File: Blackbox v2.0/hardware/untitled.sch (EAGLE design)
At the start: 40 parts, among them IC1 MEGA8-AI, IC2 7805DT, Q1 CSM-7X-DU

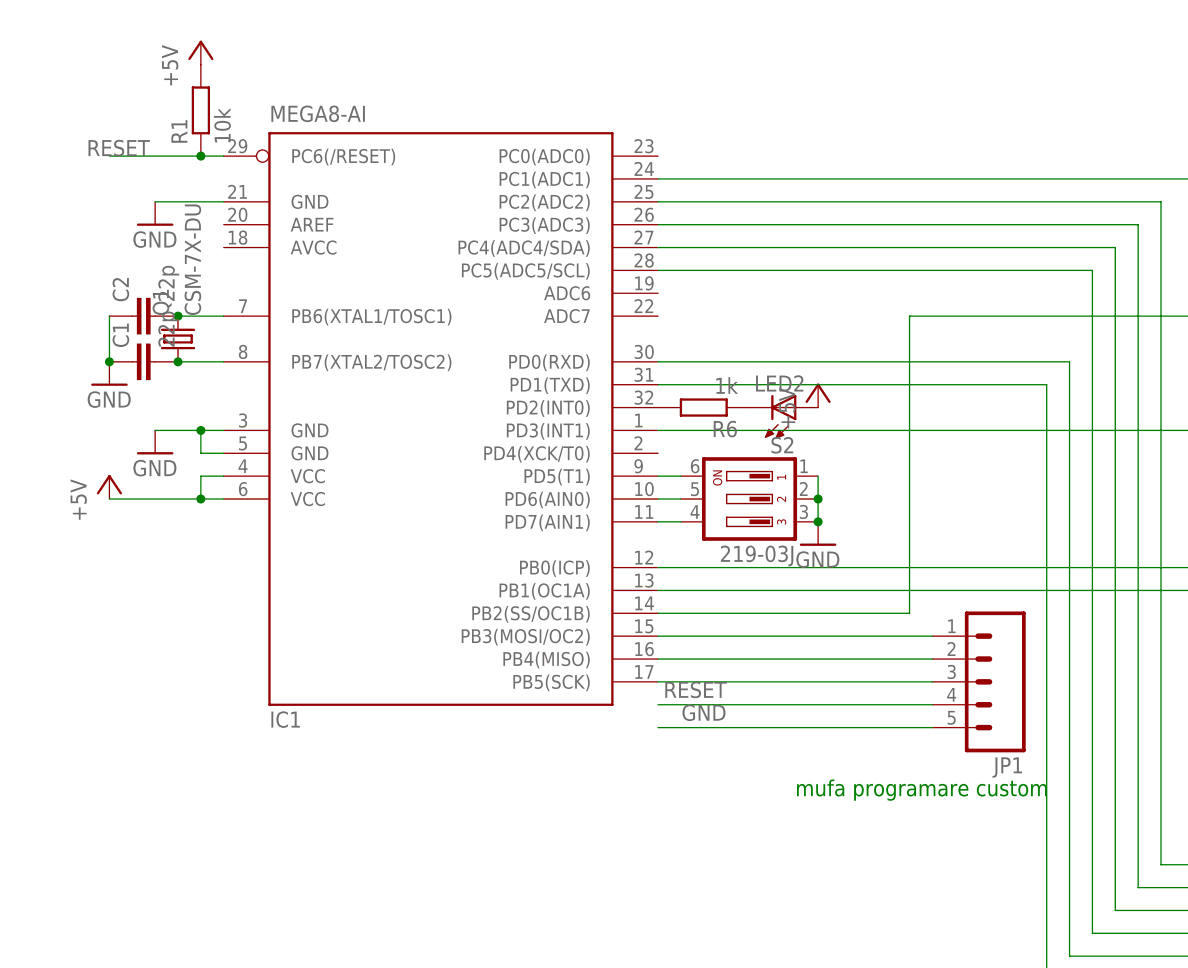
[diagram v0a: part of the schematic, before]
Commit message: Adaug placa in versiunea noua
(mufa de programare cu 6 pini si condensator pt ADC)
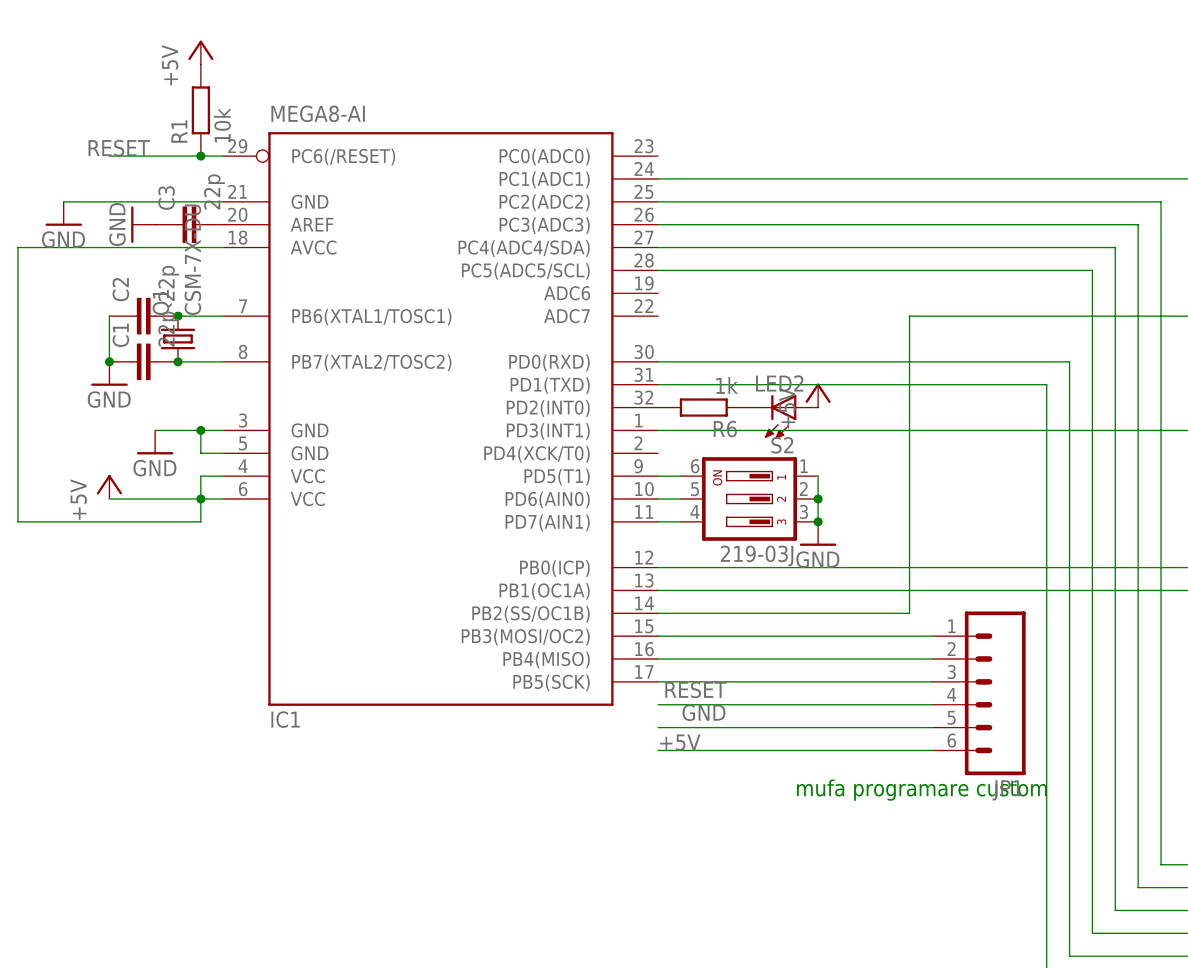
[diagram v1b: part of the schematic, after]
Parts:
- added C3: 22p, resistor:C-EUC0805
- JP1: device SparkFun-Connectors:M05PTH -> SparkFun-Connectors:M06SIP
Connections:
- new net N$38: C3.2, IC1.AREF
- net +5V: now also IC1.AVCC, JP1.6
- net GND: now also C3.1
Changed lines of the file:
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@@
 <part name="R3" library="resistor" deviceset="R-EU_" device="R0805"/>
 <part name="GND9" library="supply1" deviceset="GND" device=""/>
-<part name="JP1" library="SparkFun-Connectors" deviceset="M05" device="PTH"/>
 <part name="U$2" library="drv8833" deviceset="DRV8833-PWP" device=""/>
 <part name="GND10" library="supply1" deviceset="GND" device=""/>
@@
 <part name="GND25" library="supply1" deviceset="GND" device=""/>
 <part name="SUPPLY4" library="supply2" deviceset="V+" device=""/>
+<part name="C3" library="resistor" deviceset="C-EU" device="C0805" value="22p"/>
+<part name="GND26" library="supply1" deviceset="GND" device=""/>
+<part name="JP1" library="SparkFun-Connectors" deviceset="M06" device="SIP"/>
 </parts>
 <sheets>
@@
 <instance part="P+2" gate="1" x="50.8" y="101.6"/>
 <instance part="R1" gate="G$1" x="50.8" y="93.98" rot="R90"/>
-<instance part="GND2" gate="1" x="45.72" y="81.28"/>
+<instance part="GND2" gate="1" x="35.56" y="81.28"/>
 <instance part="Q1" gate="P" x="48.26" y="68.58" rot="R90"/>
 <instance part="C1" gate="G$1" x="43.18" y="66.04" rot="R90"/>
@@
 <instance part="R3" gate="G$1" x="195.58" y="116.84" rot="R90"/>
 <instance part="GND9" gate="1" x="195.58" y="109.22"/>
-<instance part="JP1" gate="G$1" x="139.7" y="30.48" rot="R180"/>
 <instance part="U$2" gate="G$1" x="210.82" y="68.58"/>
 <instance part="GND10" gate="1" x="213.36" y="40.64"/>
@@
 <instance part="GND25" gate="1" x="353.06" y="33.02"/>
 <instance part="SUPPLY4" gate="1" x="292.1" y="45.72"/>
+<instance part="C3" gate="G$1" x="48.26" y="81.28" rot="R90"/>
+<instance part="GND26" gate="1" x="43.18" y="81.28" rot="R270"/>
+<instance part="JP1" gate="G$1" x="137.16" y="30.48" rot="R180"/>
 </instances>
 <busses>
@@
 <pinref part="GND2" gate="1" pin="GND"/>
 <pinref part="IC1" gate="G$1" pin="GND"/>
-<wire x1="45.72" y1="83.82" x2="53.34" y2="83.82" width="0.1524" layer="91"/>
+<wire x1="35.56" y1="83.82" x2="53.34" y2="83.82" width="0.1524" layer="91"/>
 </segment>
 <segment>
@@
 <segment>
 <wire x1="101.6" y1="25.4" x2="132.08" y2="25.4" width="0.1524" layer="91"/>
+<label x="109.22" y="27.94" size="1.778" layer="95" rot="R180"/>
 <pinref part="JP1" gate="G$1" pin="5"/>
-<label x="109.22" y="27.94" size="1.778" layer="95" rot="R180"/>
 </segment>
 <segment>
@@
 <pinref part="GND25" gate="1" pin="GND"/>
 </segment>
+<segment>
+<pinref part="C3" gate="G$1" pin="1"/>
+<pinref part="GND26" gate="1" pin="GND"/>
+</segment>
 </net>
 <net name="+5V" class="0">
@@
 <wire x1="50.8" y1="53.34" x2="50.8" y2="50.8" width="0.1524" layer="91"/>
 <junction x="50.8" y="50.8"/>
+<pinref part="IC1" gate="G$1" pin="AVCC"/>
+<wire x1="53.34" y1="78.74" x2="30.48" y2="78.74" width="0.1524" layer="91"/>
+<wire x1="30.48" y1="78.74" x2="30.48" y2="48.26" width="0.1524" layer="91"/>
+<wire x1="30.48" y1="48.26" x2="50.8" y2="48.26" width="0.1524" layer="91"/>
+<wire x1="50.8" y1="48.26" x2="50.8" y2="50.8" width="0.1524" layer="91"/>
 </segment>
 <segment>
@@
 <junction x="271.78" y="12.7"/>
 </segment>
+<segment>
+<pinref part="JP1" gate="G$1" pin="6"/>
+<wire x1="132.08" y1="22.86" x2="101.6" y2="22.86" width="0.1524" layer="91"/>
+<label x="101.6" y="22.86" size="1.778" layer="95"/>
+</segment>
 </net>
 <net name="RESET" class="0">
@@
 <segment>
 <wire x1="101.6" y1="27.94" x2="132.08" y2="27.94" width="0.1524" layer="91"/>
+<label x="109.22" y="30.48" size="1.778" layer="95" rot="R180"/>
 <pinref part="JP1" gate="G$1" pin="4"/>
-<label x="109.22" y="30.48" size="1.778" layer="95" rot="R180"/>
 </segment>
 </net>
@@
 </segment>
 </net>
+<net name="N$38" class="0">
+<segment>
+<pinref part="IC1" gate="G$1" pin="AREF"/>
+<pinref part="C3" gate="G$1" pin="2"/>
+</segment>
+</net>
